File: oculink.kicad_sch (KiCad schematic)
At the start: 10 parts, among them J3 OCuLink_x4_Amphenol_G14A42121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, J4 OCuLink_x4_Amphenol_G14A42121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, J5 OCuLink_x4_Amphenol_G14A42121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

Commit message: [#100765] Update subsheets
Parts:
- removed J3, J5: OCuLink_x4_Amphenol_G14A421211112HR, antmicro-footprints:Amphenol_G14A421211112HR, symbol antmicroPciConnectors:OCuLink_x4_Amphenol_G14A421211112HR
- removed R20, R35: R_0R_0402, antmicro-footprints:R_0402_1005Metric, symbol antmicroResistors0402:R_0R_0402
- removed R33: R_1k_0402, antmicro-footprints:R_0402_1005Metric, symbol antmicroResistors0402:R_1k_0402
- removed TP5, TP6: TP_1.5mm_SMD, antmicro-footprints:TP_SMD_1.5mm, symbol antmicroTestPoints:TP_1.5mm_SMD
- added R3, R4: R_0R_0402, antmicro-footprints:R_0402_1005Metric, symbol antmicroResistors0402:R_0R_0402
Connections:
- net GND: now also J4.A11 (GND), J4.A14 (GND), J4.A17 (GND), J4.A2 (GND), J4.A20 (GND), J4.A5 (GND), J4.A8 (GND), J4.B11 (GND), J4.B14 (GND), J4.B17 (GND), J4.B2 (GND), J4.B20 (GND), J4.B5 (GND), J4.B8 (GND), J4.SH
- net at R2.2: now also J4.B10 (SDA)
- net at R1.2: now also J4.B9 (SCL)
- net at J4.A10 (~{CWAKE}): now also R4.2
- net PCIe_{x2}.CLK_P: now reaches J4.A12 (VSP1)
- net PCIe_{x2}.CLK_N: now reaches J4.A13 (VSP2)
- net PCIe_{x2}.RX0_P: now reaches J4.A3 (PER0+)
- net PCIe_{x2}.RX0_N: now reaches J4.A4 (PER0-)
- net PCIe_{x2}.RX1_P: now reaches J4.A6 (PER1+)
- net PCIe_{x2}.RX1_N: now reaches J4.A7 (PER1-)
- net at J4.B13 (~{CPRSNT}): now also R3.2
- net PCIe_{x2}.TX0_P: now reaches J4.B3 (PET0+)
- net PCIe_{x2}.TX0_N: now reaches J4.B4 (PET0-)
- net PCIe_{x2}.TX1_P: now reaches J4.B6 (PET1+)
- net PCIe_{x2}.TX1_N: now reaches J4.B7 (PET1-)
- net ~{CPRSNT} renamed SCL
- net ~{PCIE_CWAKE} renamed SDA
- no-connect marks 7 -> 8
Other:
- note removed: "JOB acts as a ROOT Device REFCLK utilizes A12(+)/A13(-)"
- moved on the sheet: J4

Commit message: [#100765] Update top level schematic, add comments
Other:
- note added: "TODO: connect PCIe indicator signals"
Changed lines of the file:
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@@
 	(generator_version "10.0")
 	(paper "A4")
+	(text "TODO: connect PCIe indicator signals\n"
+		(exclude_from_sim no)
+		(at 121.412 68.834 0)
+		(effects
+			(font
+				(size 1.27 1.27)
+				(thickness 0.254)
+				(bold yes)
+			)
+		)
+	)
 	(junction
 		(at 168.91 135.89)

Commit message: [#100765] Update schematic
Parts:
- added R12, R13: R_1k_0402, antmicro-footprints:R_0402_1005Metric, symbol antmicroResistors0402:R_1k_0402
- added R14: R_10k_0402, antmicro-footprints:R_0402_1005Metric, symbol antmicroResistors0402:R_10k_0402
- added U2: MAX3373EEKA+, antmicro-footprints:SOT-23-8, symbol antmicroLogicTranslatorsLevelShifters:MAX3373EEKA+
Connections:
- net GND: now also R12.1, R13.1, R14.1, U2.2 (GND)
- net ~{CPRSNT}: now reaches R3.1
- net ~{CPRSNT}: now also R13.2, U2.8 (IO_V_{CC}1)
- net ~{CWAKE}: now reaches R4.1
- net ~{CWAKE}: now also U2.1 (IO_V_{CC}2)
- net PCIe_{x2}.~{RST}: now reaches J4.B12 (~{PERST})
- net PCIe_{x2}.~{RST}: now also R12.2
- new net: R14.2, U2.6 (~{THREE_STATE})
- new net +1V8: U2.3 (V_{L})
- new net +3V3: U2.7 (V_{CC})
- new net ~{OCULINK_CPRSNT}: U2.5 (IO_V_{L}1)
- new net ~{OCULINK_CWAKE}: U2.4 (IO_V_{L}2)
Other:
- note added: "TODO: verify CPRSNT connection (as GPIO or pull-down)"
- note removed: "TODO: connect PCIe indicator signals"

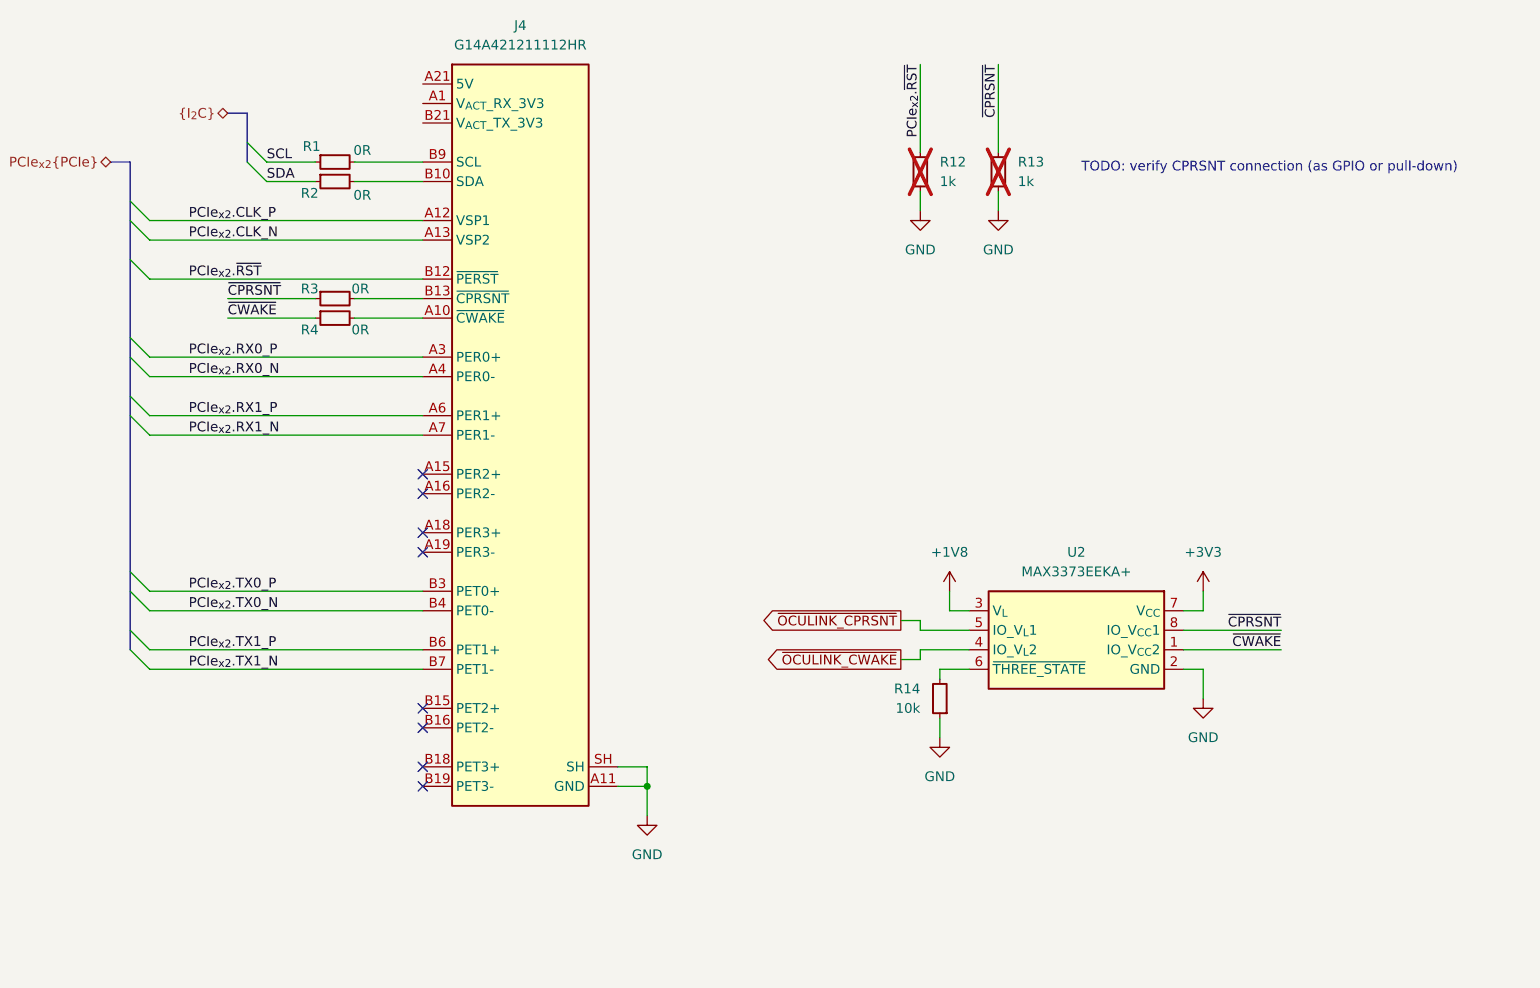
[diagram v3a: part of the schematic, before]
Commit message: [#100765] Remove I2C from OCuLink
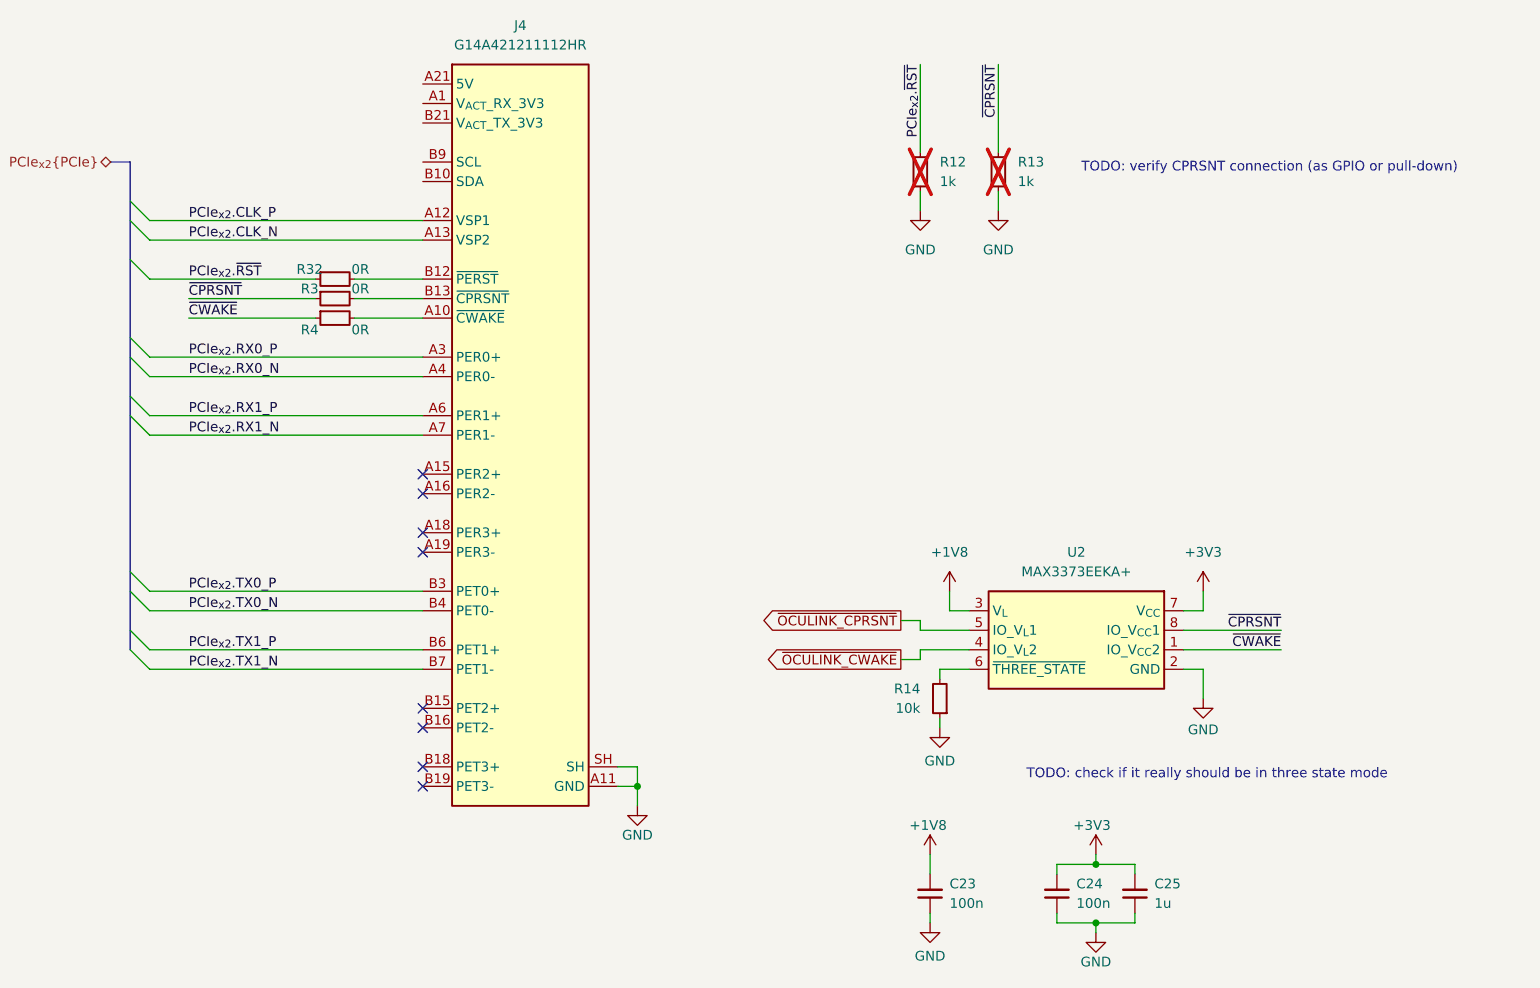
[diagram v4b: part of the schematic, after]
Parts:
- removed R1, R2: R_0R_0402, antmicro-footprints:R_0402_1005Metric, symbol antmicroResistors0402:R_0R_0402
- added C23, C24: C_100n_0402, antmicro-footprints:C_0402_1005Metric, symbol antmicroCapacitors0402:C_100n_0402
- added C25: C_1u_0402, antmicro-footprints:C_0402_1005Metric, symbol antmicroCapacitors0402:C_1u_0402
- added R32: R_0R_0402, antmicro-footprints:R_0402_1005Metric, symbol antmicroResistors0402:R_0R_0402
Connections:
- net +1V8: now also C23.2
- net +3V3: now also C24.2, C25.2
- net GND: now also C23.1, C24.1, C25.1
- net PCIe_{x2}.~{RST}: now also R32.1; no longer J4.B12 (~{PERST})
- new net: J4.B12 (~{PERST}), R32.2
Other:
- note added: "TODO: check if it really should be in three state mode"

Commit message: [#100765] Work on schematic
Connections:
- no-connect marks 8 -> 10
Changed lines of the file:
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@@
+	)
+	(no_connect
+		(at 139.7 57.15)
 	)
 	(no_connect
@@
 	)
 	(no_connect
+		(at 139.7 54.61)
+	)
+	(no_connect

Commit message: [#100765] Update schematic
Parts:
- added C19, C47: C_10u_0402, antmicro-footprints:C_0402_1005Metric, symbol antmicroCapacitors0402:C_10u_0402
- added C48, C49: C_100n_0402, antmicro-footprints:C_0402_1005Metric, symbol antmicroCapacitors0402:C_100n_0402
- added C50, C51: C_100u_0805, antmicro-footprints:C_0805_2012Metric, symbol antmicroCapacitorsmisc:C_100u_0805
- added R56, R57, R64: R_10k_0402, antmicro-footprints:R_0402_1005Metric, symbol antmicroResistors0402:R_10k_0402
- added R58: R_5k6_0402, antmicro-footprints:R_0402_1005Metric, symbol antmicroResistors0402:R_5k6_0402
- added R59: R_11k3_0402, antmicro-footprints:R_0402_1005Metric, symbol antmicroResistors0402:R_11k3_0402
- added R60, R61, R62, R63: R_0R_0402, antmicro-footprints:R_0402_1005Metric, symbol antmicroResistors0402:R_0R_0402
- added U10, U9: (no value), antmicro-footprints:TSOT23-6, symbol antmicroPMICPowerDistributionSwitchesLoadDrivers:AP22615A_TSOT26
- R13: now fitted
- R14: now not fitted
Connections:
- net +1V8: now also R64.2
- net +3V3: now also C19.2, R56.1, U9.4 (EN), U9.6 (IN)
- net GND: now also C19.1, C47.1, C48.1, C49.1, C50.1, C51.1, R58.1, R59.1, U10.2 (GND), U9.2 (GND)
- net ~{CPRSNT}: now also R62.2; no longer U2.8 (IO_V_{CC}1)
- net ~{CWAKE}: now also R63.2; no longer U2.1 (IO_V_{CC}2)
- net at R14.2, U2.6 (~{THREE_STATE}): now also R64.1
- net +3V3_OCU: now reaches J4.A1 (V_{ACT}_RX_3V3)
- net +3V3_OCU: now also J4.B21 (V_{ACT}_TX_3V3), R60.2
- net +5V_OCU: now reaches J4.A21 (5V), J4.B1 (5V)
- net +5V_OCU: now also R61.2
- new net: C48.2, C50.2, R60.1, U9.1 (OUT)
- new net: C49.2, C51.2, R61.1, U10.1 (OUT)
- new net: R58.2, U9.5 (ISET)
- new net: R59.2, U10.5 (ISET)
- new net: R56.2, U9.3 (FLG)
- new net: R63.1, U2.1 (IO_V_{CC}2)
- new net: R62.1, U2.8 (IO_V_{CC}1)
- new net: R57.2, U10.3 (FLG)
- new net +5V: C47.2, R57.1, U10.4 (EN), U10.6 (IN)
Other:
- note added: "1V8 to 3V3 LLC"
- note added: "ISET resistor value: target current limit = 0.6 A (peak OCuLink pin current) AP22615 datasheet, page 3, ISET pin description I_{LIM} (A) = 6800 / R_{LIM} (Ohms) 0.6 A = 6800 / R_{LIM} Ohms R_{LIM} = 6800 / 0.6 = 11333 Ohms ~= 11.3 kOhms"
- note added: "ISET resistor value: target current limit = 1.2 A (2x peak OCuLink pin current) AP22615 datasheet, page 3, ISET pin description I_{LIM} (A) = 6800 / R_{LIM} (Ohms) 1.2 A = 6800 / R_{LIM} Ohms R_{LIM} = 6800 / 1.2 = 5666 Ohms ~= 5.6 kOhms real current limit ~= 1.214 A"
- note added: "OCuLink Connector"
- note added: "OCuLink e-fuses"
- note removed: "TODO: check if it really should be in three state mode"
- note removed: "TODO: verify CPRSNT connection (as GPIO or pull-down)"
- moved on the sheet: C23, C24, C25, J4, R12, R3, R32, R4, U2

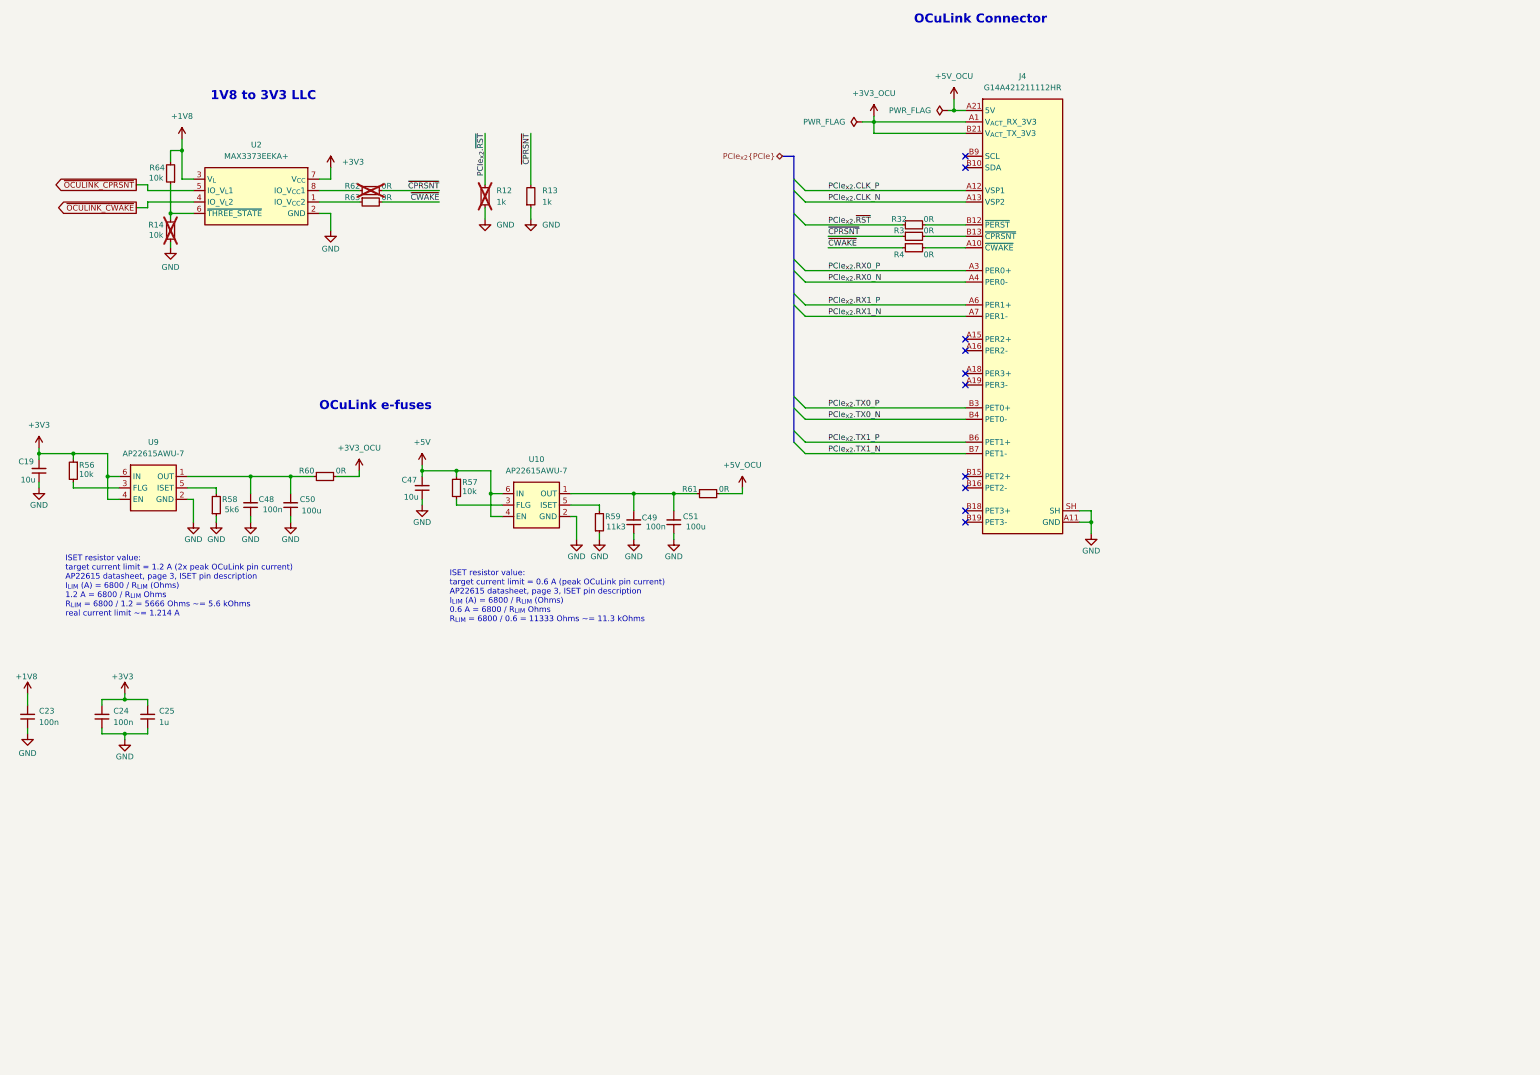
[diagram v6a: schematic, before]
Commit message: [#100765] Change sheet format to A3, update schematic
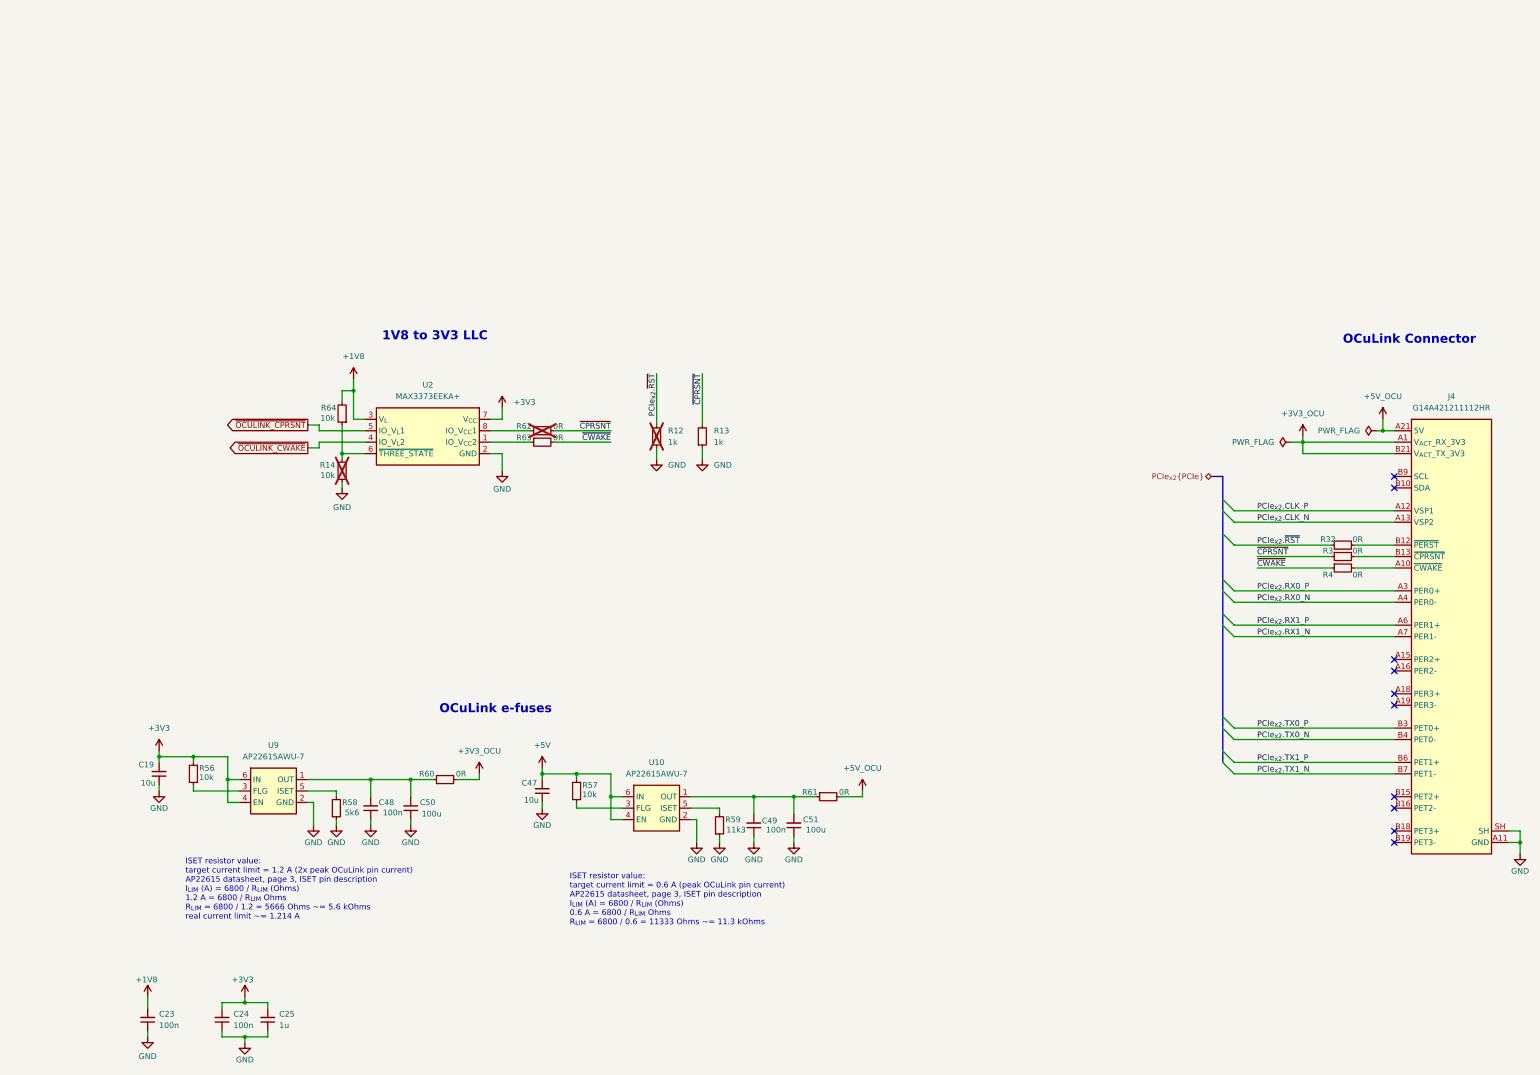
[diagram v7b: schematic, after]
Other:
- company: (none) -> Antmicro
- title: (none) -> antmicro-jetson-orin-baseboard-pcie-switch-expansion-hw
- moved on the sheet: C19, C23, C24, C25, C47, C48, C49, C50, C51, J4, R12, R13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
